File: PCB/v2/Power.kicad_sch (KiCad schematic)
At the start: 19 parts

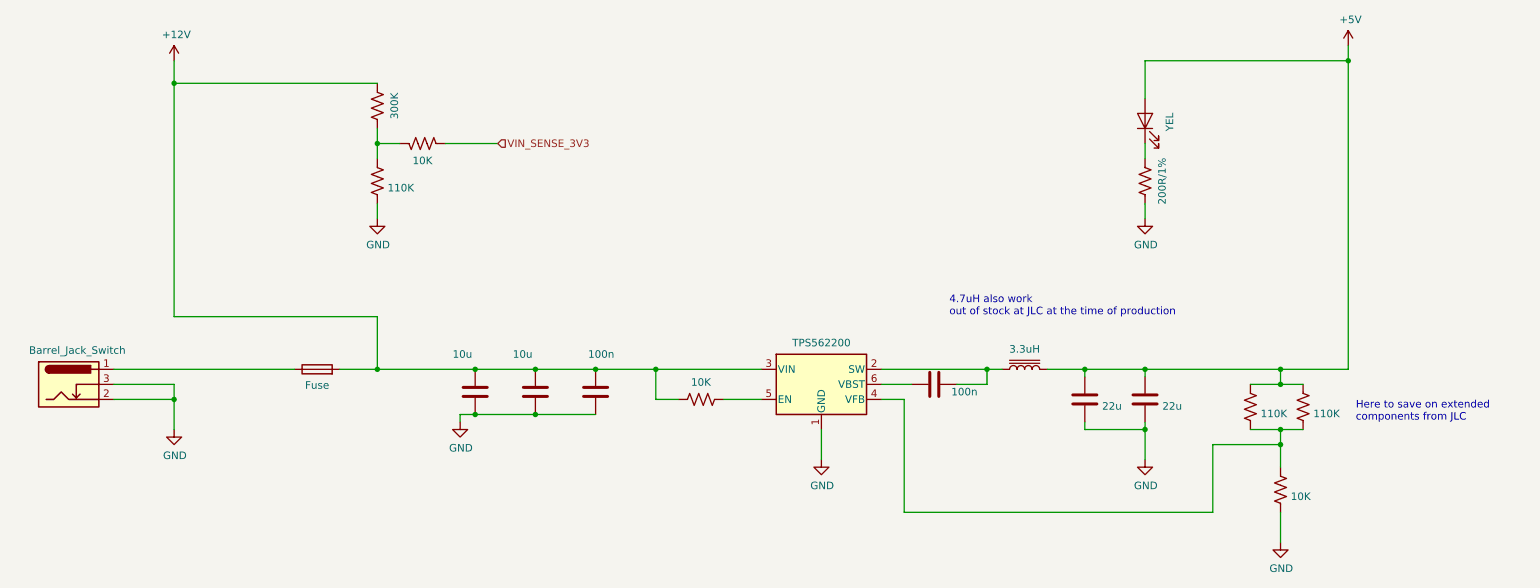
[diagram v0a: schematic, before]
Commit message: WIP updated symbols for tmc5106
Updated footprint for tmc5106,
need to check how motor wiring is done, might be wired up stupid before and that's gonna be sad
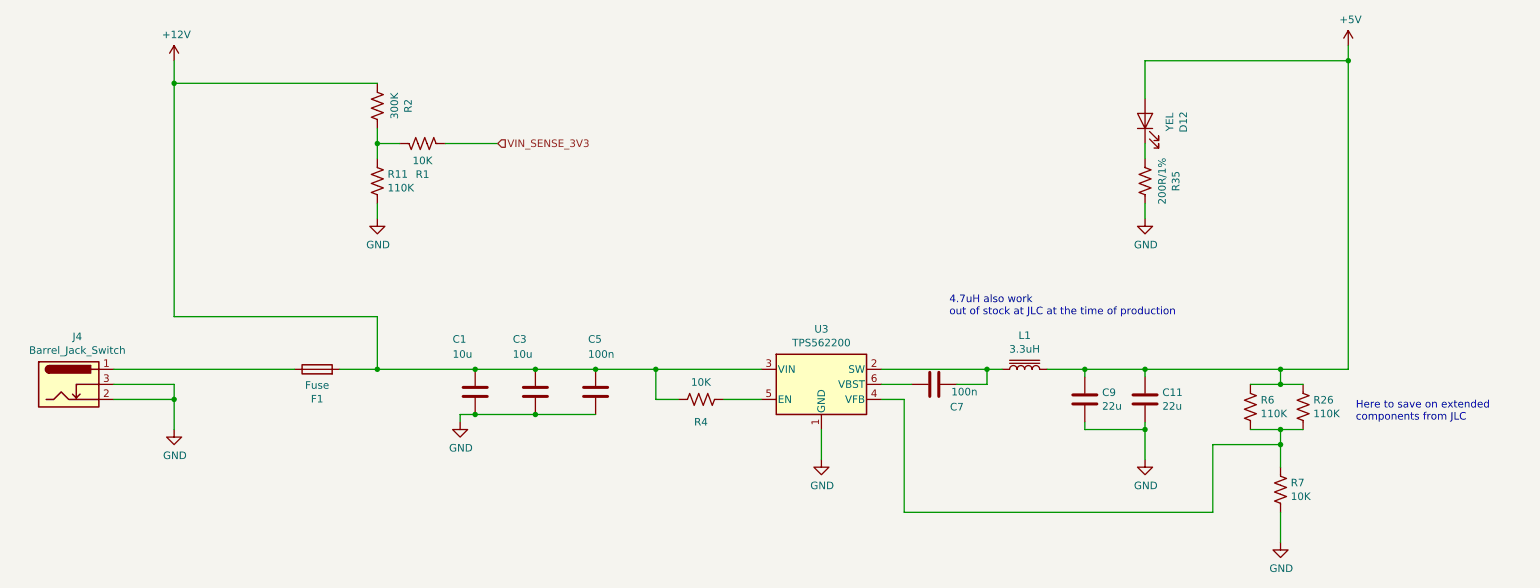
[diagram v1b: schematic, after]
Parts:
- gave numbers to parts that had none: 19
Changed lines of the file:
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@@
   (symbol (lib_id "MMTK-rescue:R_US-Device-MMTK-rescue-MMTK-rescue") (at 143.51 123.19 90) (unit 1)
     (in_bom yes) (on_board yes)
-    (property "Reference" "" (id 0) (at 143.51 127 90))
+    (property "Reference" "R4" (id 0) (at 143.51 127 90))
     (property "Value" "10K" (id 1) (at 143.51 120.2944 90))
     (property "Footprint" "Resistor_SMD:R_0603_1608Metric" (id 2) (at 143.764 122.174 90)
@@
   (symbol (lib_id "MMTK-rescue:GND-power-MMTK-rescue-MMTK-rescue") (at 163.83 133.35 0) (unit 1)
     (in_bom yes) (on_board yes)
-    (property "Reference" "" (id 0) (at 163.83 139.7 0)
+    (property "Reference" "#PWR0104" (id 0) (at 163.83 139.7 0)
       (effects (font (size 1.27 1.27)) hide)
     )
@@
   (symbol (lib_id "MMTK-rescue:C-Device-MMTK-rescue-MMTK-rescue") (at 105.41 121.92 0) (unit 1)
     (in_bom yes) (on_board yes)
-    (property "Reference" "" (id 0) (at 101.6 113.03 0)
+    (property "Reference" "C1" (id 0) (at 101.6 113.03 0)
       (effects (font (size 1.27 1.27)) (justify left))
     )
@@
   (symbol (lib_id "MMTK-rescue:C-Device-MMTK-rescue-MMTK-rescue") (at 115.57 121.92 0) (unit 1)
     (in_bom yes) (on_board yes)
-    (property "Reference" "" (id 0) (at 111.76 113.03 0)
+    (property "Reference" "C3" (id 0) (at 111.76 113.03 0)
       (effects (font (size 1.27 1.27)) (justify left))
     )
@@
   (symbol (lib_id "MMTK-rescue:C-Device-MMTK-rescue-MMTK-rescue") (at 125.73 121.92 0) (unit 1)
     (in_bom yes) (on_board yes)
-    (property "Reference" "" (id 0) (at 124.46 113.03 0)
+    (property "Reference" "C5" (id 0) (at 124.46 113.03 0)
       (effects (font (size 1.27 1.27)) (justify left))
     )
@@
   (symbol (lib_id "MMTK-rescue:GND-power-MMTK-rescue-MMTK-rescue") (at 102.87 127 0) (unit 1)
     (in_bom yes) (on_board yes)
-    (property "Reference" "" (id 0) (at 102.87 133.35 0)
+    (property "Reference" "#PWR0105" (id 0) (at 102.87 133.35 0)
       (effects (font (size 1.27 1.27)) hide)
     )
@@
   (symbol (lib_id "MMTK-rescue:C-Device-MMTK-rescue-MMTK-rescue") (at 182.88 120.65 270) (unit 1)
     (in_bom yes) (on_board yes)
-    (property "Reference" "" (id 0) (at 186.69 124.46 90))
+    (property "Reference" "C7" (id 0) (at 186.69 124.46 90))
     (property "Value" "100n" (id 1) (at 187.96 121.92 90))
     (property "Footprint" "Capacitor_SMD:C_0603_1608Metric" (id 2) (at 179.07 121.6152 0)
@@
   (symbol (lib_id "MMTK-rescue:C-Device-MMTK-rescue-MMTK-rescue") (at 218.44 123.19 0) (unit 1)
     (in_bom yes) (on_board yes)
-    (property "Reference" "" (id 0) (at 221.361 122.0216 0)
+    (property "Reference" "C11" (id 0) (at 221.361 122.0216 0)
       (effects (font (size 1.27 1.27)) (justify left))
     )
@@
   (symbol (lib_id "MMTK-rescue:GND-power-MMTK-rescue-MMTK-rescue") (at 218.44 133.35 0) (unit 1)
     (in_bom yes) (on_board yes)
-    (property "Reference" "" (id 0) (at 218.44 139.7 0)
+    (property "Reference" "#PWR0106" (id 0) (at 218.44 139.7 0)
       (effects (font (size 1.27 1.27)) hide)
     )
@@
   (symbol (lib_id "MMTK-rescue:R_US-Device-MMTK-rescue-MMTK-rescue") (at 241.3 138.43 0) (unit 1)
     (in_bom yes) (on_board yes)
-    (property "Reference" "" (id 0) (at 243.0272 137.2616 0)
+    (property "Reference" "R7" (id 0) (at 243.0272 137.2616 0)
       (effects (font (size 1.27 1.27)) (justify left))
     )
@@
   (symbol (lib_id "MMTK-rescue:GND-power-MMTK-rescue-MMTK-rescue") (at 241.3 147.32 0) (unit 1)
     (in_bom yes) (on_board yes)
-    (property "Reference" "" (id 0) (at 241.3 153.67 0)
+    (property "Reference" "#PWR0107" (id 0) (at 241.3 153.67 0)
       (effects (font (size 1.27 1.27)) hide)
     )
@@
   (symbol (lib_id "MMTK-rescue:L_Core_Iron-Device-MMTK-rescue-MMTK-rescue") (at 198.12 118.11 90) (unit 1)
     (in_bom yes) (on_board yes)
-    (property "Reference" "" (id 0) (at 198.12 112.395 90))
+    (property "Reference" "L1" (id 0) (at 198.12 112.395 90))
     (property "Value" "3.3uH" (id 1) (at 198.12 114.7064 90))
     (property "Footprint" "Inductor_SMD:L_Bourns_SRP7028A_7.3x6.6mm" (id 2) (at 198.12 118.11 0)
@@
   (symbol (lib_id "MMTK-rescue:C-Device-MMTK-rescue-MMTK-rescue") (at 208.28 123.19 0) (unit 1)
     (in_bom yes) (on_board yes)
-    (property "Reference" "" (id 0) (at 211.201 122.0216 0)
+    (property "Reference" "C9" (id 0) (at 211.201 122.0216 0)
       (effects (font (size 1.27 1.27)) (justify left))
     )
@@
   (symbol (lib_id "MMTK-rescue:R_US-Device-MMTK-rescue-MMTK-rescue") (at 88.9 73.66 180) (unit 1)
     (in_bom yes) (on_board yes)
-    (property "Reference" "" (id 0) (at 94.107 73.66 90))
+    (property "Reference" "R2" (id 0) (at 94.107 73.66 90))
     (property "Value" "300K" (id 1) (at 91.7956 73.66 90))
     (property "Footprint" "Resistor_SMD:R_0603_1608Metric" (id 2) (at 87.884 73.406 90)
@@
   (symbol (lib_id "MMTK-rescue:GND-power-MMTK-rescue-MMTK-rescue") (at 88.9 92.71 0) (unit 1)
     (in_bom yes) (on_board yes)
-    (property "Reference" "" (id 0) (at 88.9 99.06 0)
+    (property "Reference" "#PWR0128" (id 0) (at 88.9 99.06 0)
       (effects (font (size 1.27 1.27)) hide)
     )
@@
   (symbol (lib_id "MMTK-rescue:R_US-Device-MMTK-rescue-MMTK-rescue") (at 96.52 80.01 270) (mirror x) (unit 1)
     (in_bom yes) (on_board yes)
-    (property "Reference" "" (id 0) (at 96.52 85.217 90))
+    (property "Reference" "R1" (id 0) (at 96.52 85.217 90))
     (property "Value" "10K" (id 1) (at 96.52 82.9056 90))
     (property "Footprint" "Resistor_SMD:R_0603_1608Metric" (id 2) (at 96.266 78.994 90)
@@
   (symbol (lib_id "MMTK-rescue:+5V-power-MMTK-rescue-MMTK-rescue") (at 252.73 63.5 0) (unit 1)
     (in_bom yes) (on_board yes)
-    (property "Reference" "" (id 0) (at 252.73 67.31 0)
+    (property "Reference" "#PWR0144" (id 0) (at 252.73 67.31 0)
       (effects (font (size 1.27 1.27)) hide)
     )
@@
   (symbol (lib_id "MMTK-rescue:GND-power-MMTK-rescue-MMTK-rescue") (at 54.61 128.27 0) (unit 1)
     (in_bom yes) (on_board yes)
-    (property "Reference" "" (id 0) (at 54.61 134.62 0)
+    (property "Reference" "#PWR0146" (id 0) (at 54.61 134.62 0)
       (effects (font (size 1.27 1.27)) hide)
     )
@@
   (symbol (lib_id "MMTK-rescue:Barrel_Jack_Switch-Connector-MMTK-rescue-MMTK-rescue") (at 36.83 120.65 0) (unit 1)
     (in_bom yes) (on_board yes)
-    (property "Reference" "" (id 0) (at 38.2778 112.5982 0))
+    (property "Reference" "J4" (id 0) (at 38.2778 112.5982 0))
     (property "Value" "Barrel_Jack_Switch" (id 1) (at 38.2778 114.9096 0))
     (property "Footprint" "Connector_BarrelJack:BarrelJack_Horizontal" (id 2) (at 38.1 121.666 0)
@@
   (symbol (lib_id "MMTK-rescue:TPS562200-Regulator_Switching-MMTK-rescue-MMTK-rescue") (at 163.83 120.65 0) (unit 1)
     (in_bom yes) (on_board yes)
-    (property "Reference" "" (id 0) (at 163.83 111.3282 0))
+    (property "Reference" "U3" (id 0) (at 163.83 111.3282 0))
     (property "Value" "TPS562200" (id 1) (at 163.83 113.6396 0))
     (property "Footprint" "Package_TO_SOT_SMD:SOT-23-6" (id 2) (at 165.1 127 0)
@@
   (symbol (lib_id "MMTK-rescue:+12V-power-MMTK-rescue-MMTK-rescue") (at 54.61 66.04 0) (unit 1)
     (in_bom yes) (on_board yes)
-    (property "Reference" "" (id 0) (at 54.61 69.85 0)
+    (property "Reference" "#PWR0145" (id 0) (at 54.61 69.85 0)
       (effects (font (size 1.27 1.27)) hide)
     )
@@
   (symbol (lib_id "MMTK-rescue:Fuse-Device-MMTK-rescue-MMTK-rescue") (at 78.74 118.11 90) (unit 1)
     (in_bom yes) (on_board yes)
-    (property "Reference" "" (id 0) (at 78.74 123.1138 90))
+    (property "Reference" "F1" (id 0) (at 78.74 123.1138 90))
     (property "Value" "Fuse" (id 1) (at 78.74 120.8024 90))
     (property "Footprint" "Fuse:Fuse_2920_7451Metric" (id 2) (at 78.74 119.888 90)
@@
   (symbol (lib_id "MMTK-rescue:LED-Device-MMTK-rescue-MMTK-rescue") (at 218.44 76.2 90) (unit 1)
     (in_bom yes) (on_board yes)
-    (property "Reference" "" (id 0) (at 224.917 76.3778 0))
+    (property "Reference" "D12" (id 0) (at 224.917 76.3778 0))
     (property "Value" "YEL" (id 1) (at 222.6056 76.3778 0))
     (property "Footprint" "LED_SMD:LED_0603_1608Metric" (id 2) (at 218.44 76.2 0)
@@
   (symbol (lib_id "MMTK-rescue:GND-power-MMTK-rescue-MMTK-rescue") (at 218.44 92.71 0) (unit 1)
     (in_bom yes) (on_board yes)
-    (property "Reference" "" (id 0) (at 218.44 99.06 0)
+    (property "Reference" "#PWR0159" (id 0) (at 218.44 99.06 0)
       (effects (font (size 1.27 1.27)) hide)
     )
@@
   (symbol (lib_id "MMTK-rescue:R_US-Device-MMTK-rescue-MMTK-rescue") (at 236.22 124.46 0) (unit 1)
     (in_bom yes) (on_board yes)
-    (property "Reference" "" (id 0) (at 237.9472 123.2916 0)
+    (property "Reference" "R6" (id 0) (at 237.9472 123.2916 0)
       (effects (font (size 1.27 1.27)) (justify left))
     )
@@
   (symbol (lib_id "MMTK-rescue:R_US-Device-MMTK-rescue-MMTK-rescue") (at 245.11 124.46 0) (unit 1)
     (in_bom yes) (on_board yes)
-    (property "Reference" "" (id 0) (at 246.8372 123.2916 0)
+    (property "Reference" "R26" (id 0) (at 246.8372 123.2916 0)
       (effects (font (size 1.27 1.27)) (justify left))
     )
@@
   (symbol (lib_id "MMTK-rescue:R_US-Device-MMTK-rescue-MMTK-rescue") (at 218.44 86.36 180) (unit 1)
     (in_bom yes) (on_board yes)
-    (property "Reference" "" (id 0) (at 223.647 86.36 90))
+    (property "Reference" "R35" (id 0) (at 223.647 86.36 90))
     (property "Value" "200R/1%" (id 1) (at 221.3356 86.36 90))
     (property "Footprint" "Resistor_SMD:R_0603_1608Metric" (id 2) (at 217.424 86.106 90)
@@
   (symbol (lib_id "MMTK-rescue:R_US-Device-MMTK-rescue-MMTK-rescue") (at 88.9 86.36 0) (unit 1)
     (in_bom yes) (on_board yes)
-    (property "Reference" "" (id 0) (at 90.6272 85.1916 0)
-      (effects (font (size 1.27 1.27)) (justify left))
-    )
+    (property "Reference" "R11" (id 0) (at 90.6272 85.1916 0)
+      (effects (font (size 1.27 1.27)) (justify left))
+    )
